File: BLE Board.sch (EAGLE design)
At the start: 34 parts, among them IC1 TM4C123GH6PM, IC2 TPS6300, J1 SAMTEC-FTSH-105-01-X-DVJ, Q1 NX5032GA

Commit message: First arrangement of components
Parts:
- removed PC4, PF0: (no value), EE445L:B3F-1052
- removed R6: 10k, EE445L:RESISTORR0402
- added C17, C19: 0.1uF, EE445L:CAPACITORC0402K
- added C18-T, C20-T: 4.7uF, EE445L:CAPACITORC0402K
- added R5: 10k, EE445L:RESISTORR0402
- added SW-PC4, SW-PF0: (no value), EE445L:B3F-1052
- C13, C14, C16: value 0.01uF -> 10uF
- C15: value 0.01uF -> 0.1uF
- R3: value 1M -> 100
- renumbered C4 to C4-T, J1 to BLE-DEBUG, Q1 to CRYS, S1 to RST, U$1 to BLE, U$2 to ON/OFF, U$3 to JTAG
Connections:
- net +3V3: now also C17.2, C18-T.2, C19.1, C20-T.1, SW-PC4.P, SW-PC4.P1, SW-PF0.P, SW-PF0.P1; no longer PC4.P, PC4.P1, PF0.P, PF0.P1
- net GND: now also C17.1, C18-T.1, C19.2, C20-T.2, R5.2; no longer R6.2
- net PF3: now also R5.1, SW-PF0.S, SW-PF0.S1; no longer PF0.S, PF0.S1, R6.1
- net PF4: now also SW-PC4.S, SW-PC4.S1; no longer PC4.S, PC4.S1
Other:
- moved on the sheet: DIS1, R4

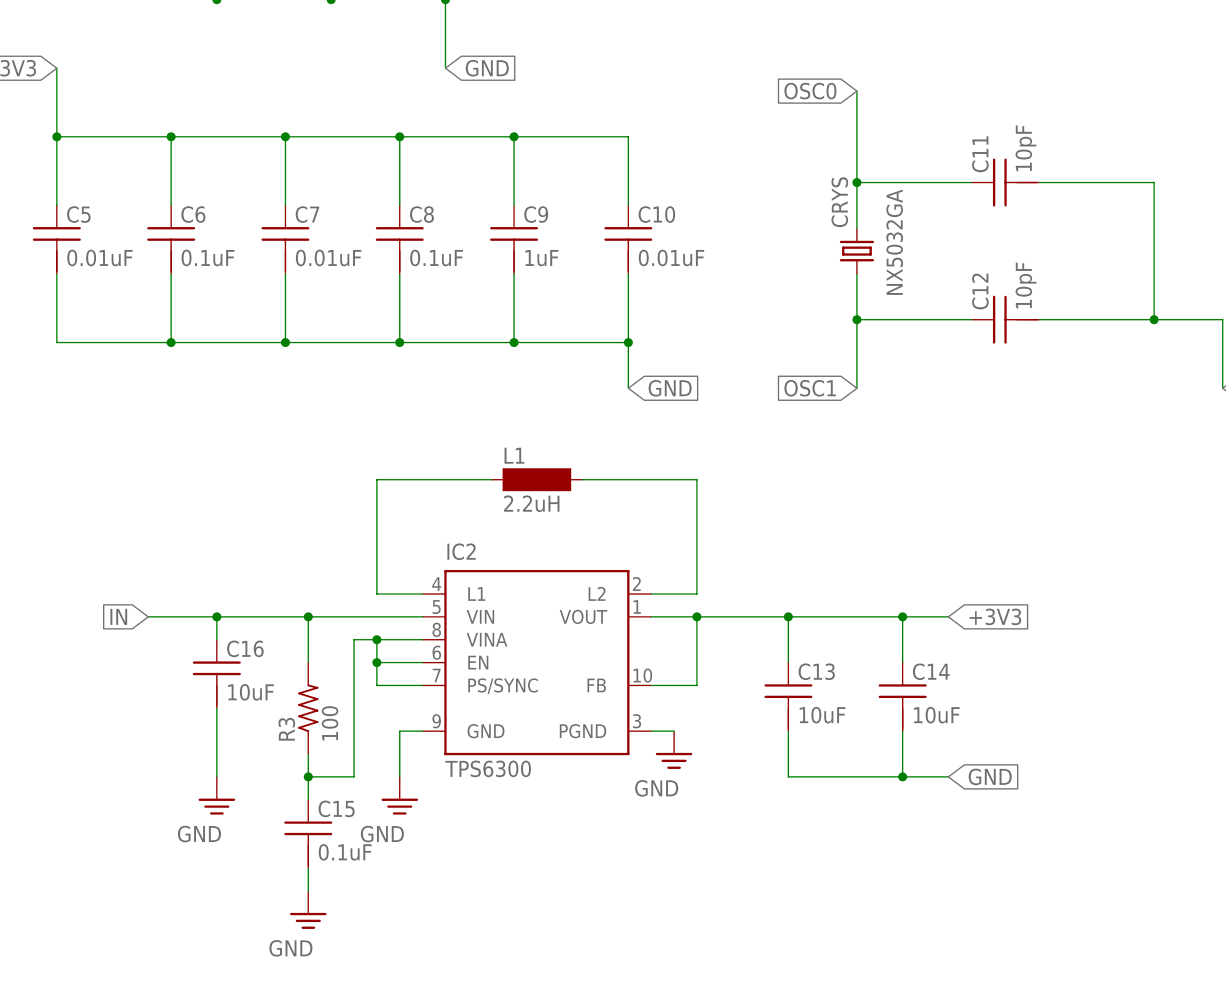
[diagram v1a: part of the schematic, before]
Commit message: Moved power reg., changed some parts
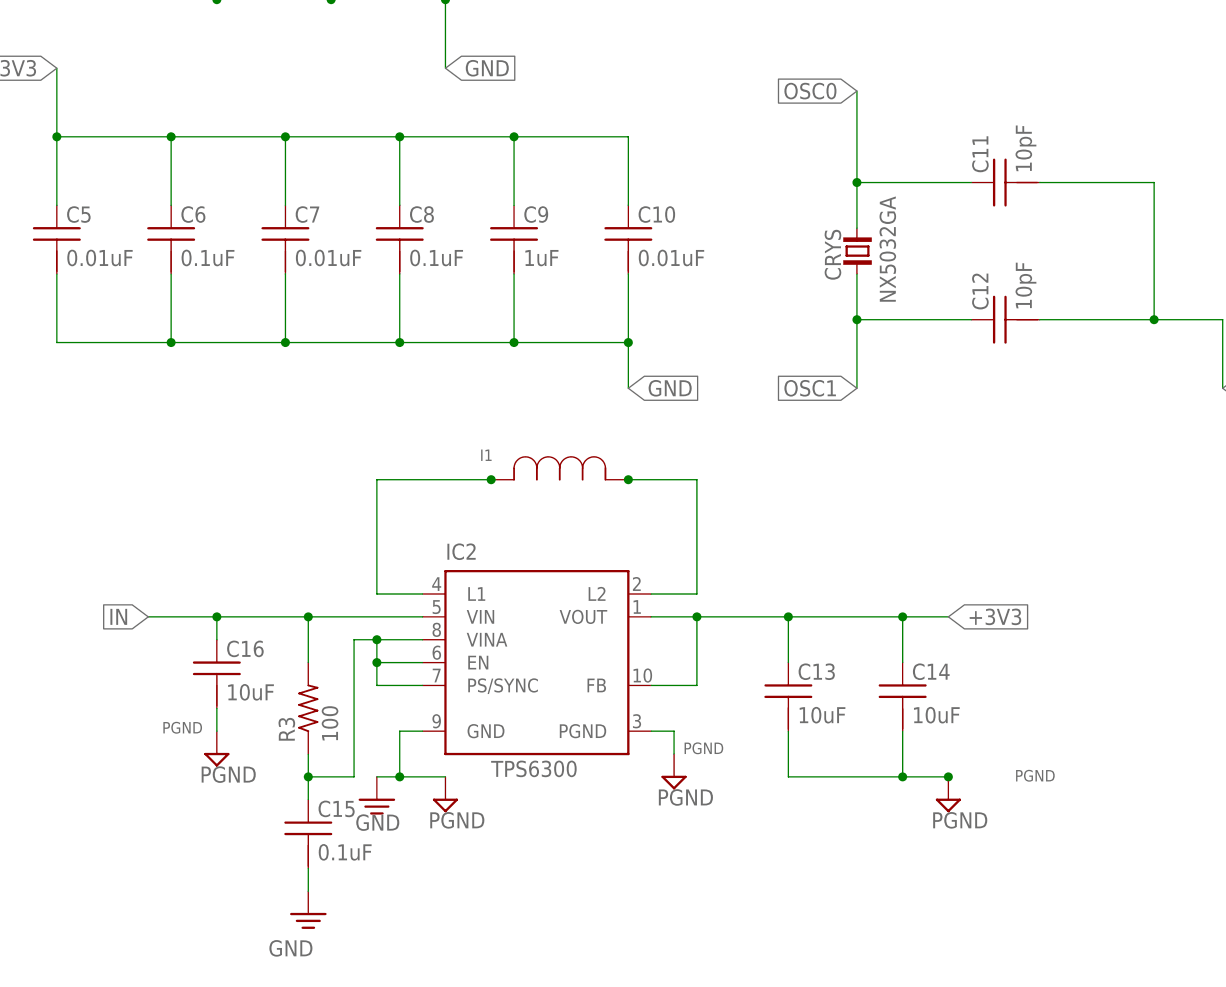
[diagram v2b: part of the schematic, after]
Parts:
- removed L1: 2.2uH, inductor-neosid:MS50
- added I1: (no value), 445L_final:IND_TPS
- CRYS: device EE445L:NX5032GA -> NX5032GA:NX5032GA
- R2, R3: device EE445L:RESISTORR0603 -> EE445L:RESISTORR0402
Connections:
- new net PGND: C13.2, C14.2, C16.2, IC2G$1.PGND
- net GND: no longer C13.2, C14.2, C16.2, IC2G$1.PGND
- net N$3: now also I1.2; no longer L1.1
- net N$4: now also I1.1; no longer L1.2

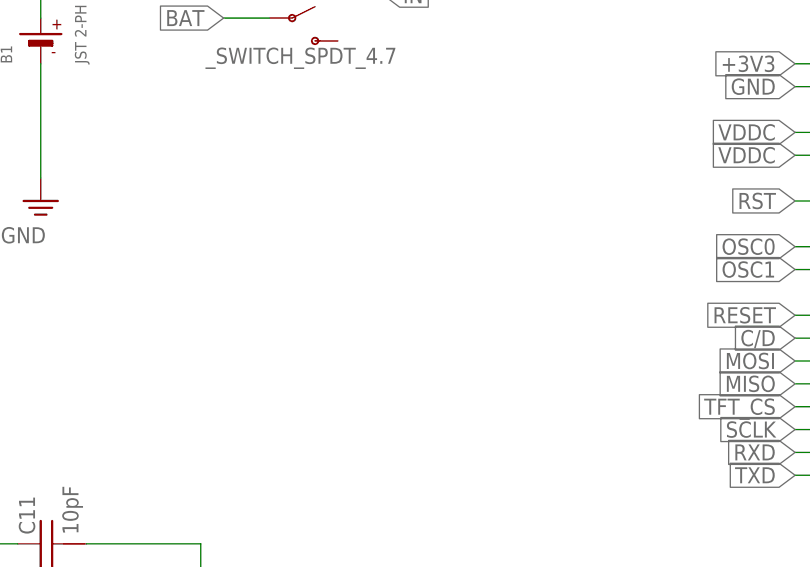
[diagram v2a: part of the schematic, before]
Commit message: 0603 cap/res, add test pts for gnd/pwr
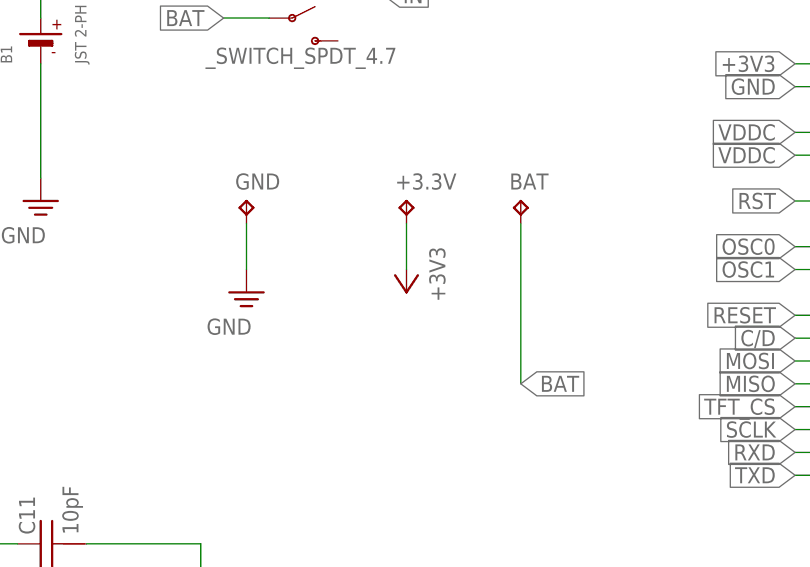
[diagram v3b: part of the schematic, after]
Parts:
- added +3.3V, BAT, GND: TP_KEYSTONE500X, EE445L:TP_KEYSTONE500X
- C1, C10, C11, C12, C13, C14, C15, C16, C17, C18-T, C19, C2, C20-T, C3, C4-T, C5, C6, C7, C8, C9: device EE445L:CAPACITORC0402K -> EE445L:CAPACITORC0603K
- R1, R2, R3, R4, R5: device EE445L:RESISTORR0402 -> EE445L:RESISTORR0603
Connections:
- net +3V3: now also +3.3V.TP
- net BAT: now also BAT.TP
- net GND: now also GND.TP
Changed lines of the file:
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@@
 <setting verticaltext="up"/>
 </settings>
-<grid distance="10" unitdist="mil" unit="mil" style="lines" multiple="1" display="no" altdistance="0.01" altunitdist="inch" altunit="inch"/>
+<grid distance="0.1" unitdist="inch" unit="inch" style="lines" multiple="1" display="no" altdistance="0.01" altunitdist="inch" altunit="inch"/>
 <layers>
 <layer number="1" name="Top" color="4" fill="1" visible="no" active="no"/>
@@
 <part name="+3V1" library="EE445L" deviceset="+3V3" device=""/>
 <part name="SUPPLY1" library="EE445L" deviceset="GND" device=""/>
-<part name="C1" library="EE445L" deviceset="CAPACITOR" device="C0402K" value="0.1uF"/>
-<part name="C2" library="EE445L" deviceset="CAPACITOR" device="C0402K" value="0.1uF"/>
-<part name="C3" library="EE445L" deviceset="CAPACITOR" device="C0402K" value="1uF"/>
-<part name="C5" library="EE445L" deviceset="CAPACITOR" device="C0402K" value="0.01uF"/>
-<part name="C6" library="EE445L" deviceset="CAPACITOR" device="C0402K" value="0.1uF"/>
-<part name="C7" library="EE445L" deviceset="CAPACITOR" device="C0402K" value="0.01uF"/>
-<part name="C8" library="EE445L" deviceset="CAPACITOR" device="C0402K" value="0.1uF"/>
-<part name="C9" library="EE445L" deviceset="CAPACITOR" device="C0402K" value="1uF"/>
-<part name="C10" library="EE445L" deviceset="CAPACITOR" device="C0402K" value="0.01uF"/>
+<part name="C1" library="EE445L" deviceset="CAPACITOR" device="C0603K" value="0.1uF"/>
+<part name="C2" library="EE445L" deviceset="CAPACITOR" device="C0603K" value="0.1uF"/>
+<part name="C3" library="EE445L" deviceset="CAPACITOR" device="C0603K" value="1uF"/>
+<part name="C5" library="EE445L" deviceset="CAPACITOR" device="C0603K" value="0.01uF"/>
+<part name="C6" library="EE445L" deviceset="CAPACITOR" device="C0603K" value="0.1uF"/>
+<part name="C7" library="EE445L" deviceset="CAPACITOR" device="C0603K" value="0.01uF"/>
+<part name="C8" library="EE445L" deviceset="CAPACITOR" device="C0603K" value="0.1uF"/>
+<part name="C9" library="EE445L" deviceset="CAPACITOR" device="C0603K" value="1uF"/>
+<part name="C10" library="EE445L" deviceset="CAPACITOR" device="C0603K" value="0.01uF"/>
 <part name="RST" library="EE445L" deviceset="B3F-1052" device=""/>
-<part name="R1" library="EE445L" deviceset="RESISTOR" device="R0402" value="10k"/>
-<part name="C11" library="EE445L" deviceset="CAPACITOR" device="C0402K" value="10pF"/>
-<part name="C12" library="EE445L" deviceset="CAPACITOR" device="C0402K" value="10pF"/>
-<part name="C4-T" library="EE445L" deviceset="CAPACITOR" device="C0402K" value="2.2uF"/>
-<part name="C13" library="EE445L" deviceset="CAPACITOR" device="C0402K" value="10uF"/>
-<part name="C14" library="EE445L" deviceset="CAPACITOR" device="C0402K" value="10uF"/>
-<part name="C15" library="EE445L" deviceset="CAPACITOR" device="C0402K" value="0.1uF"/>
-<part name="C16" library="EE445L" deviceset="CAPACITOR" device="C0402K" value="10uF"/>
+<part name="R1" library="EE445L" deviceset="RESISTOR" device="R0603" value="10k"/>
+<part name="C11" library="EE445L" deviceset="CAPACITOR" device="C0603K" value="10pF"/>
+<part name="C12" library="EE445L" deviceset="CAPACITOR" device="C0603K" value="10pF"/>
+<part name="C4-T" library="EE445L" deviceset="CAPACITOR" device="C0603K" value="2.2uF"/>
+<part name="C13" library="EE445L" deviceset="CAPACITOR" device="C0603K" value="10uF"/>
+<part name="C14" library="EE445L" deviceset="CAPACITOR" device="C0603K" value="10uF"/>
+<part name="C15" library="EE445L" deviceset="CAPACITOR" device="C0603K" value="0.1uF"/>
+<part name="C16" library="EE445L" deviceset="CAPACITOR" device="C0603K" value="10uF"/>
 <part name="SUPPLY3" library="EE445L" deviceset="GND" device=""/>
 <part name="B1" library="microbuilder" deviceset="BATTERY" device="" value="JST 2-PH"/>
@@
 <part name="DIS1" library="EE445L" deviceset="ST7735" device=""/>
 <part name="SW-PC4" library="EE445L" deviceset="B3F-1052" device=""/>
-<part name="R4" library="EE445L" deviceset="RESISTOR" device="R0402" value="10k"/>
+<part name="R4" library="EE445L" deviceset="RESISTOR" device="R0603" value="10k"/>
 <part name="SW-PF0" library="EE445L" deviceset="B3F-1052" device=""/>
-<part name="R5" library="EE445L" deviceset="RESISTOR" device="R0402" value="10k"/>
+<part name="R5" library="EE445L" deviceset="RESISTOR" device="R0603" value="10k"/>
 <part name="BLE-DEBUG" library="SAMTEC-FTSH-105-01-X-DV" deviceset="SAMTEC-FTSH-105-01-X-DV" device="J"/>
 <part name="BLE" library="zyongye" deviceset="BGM220P" device=""/>
 <part name="ON/OFF" library="Z" deviceset="_SWITCH_SPDT_4.7" device=""/>
 <part name="JTAG" library="Z" deviceset="JTAG_SERIAL" device=""/>
-<part name="C19" library="EE445L" deviceset="CAPACITOR" device="C0402K" value="0.1uF"/>
-<part name="C20-T" library="EE445L" deviceset="CAPACITOR" device="C0402K" value="4.7uF"/>
-<part name="C17" library="EE445L" deviceset="CAPACITOR" device="C0402K" value="0.1uF"/>
-<part name="C18-T" library="EE445L" deviceset="CAPACITOR" device="C0402K" value="4.7uF"/>
+<part name="C19" library="EE445L" deviceset="CAPACITOR" device="C0603K" value="0.1uF"/>
+<part name="C20-T" library="EE445L" deviceset="CAPACITOR" device="C0603K" value="4.7uF"/>
+<part name="C17" library="EE445L" deviceset="CAPACITOR" device="C0603K" value="0.1uF"/>
+<part name="C18-T" library="EE445L" deviceset="CAPACITOR" device="C0603K" value="4.7uF"/>
 <part name="I1" library="445L_final" deviceset="IND_TPS" device=""/>
 <part name="SUPPLY7" library="supply2" library_urn="urn:adsk.eagle:library:372" deviceset="GND" device="" value="PGND"/>
@@
 <part name="SUPPLY9" library="supply2" library_urn="urn:adsk.eagle:library:372" deviceset="GND" device="" value="PGND"/>
 <part name="SUPPLY10" library="supply2" library_urn="urn:adsk.eagle:library:372" deviceset="GND" device="" value="PGND"/>
-<part name="R3" library="EE445L" deviceset="RESISTOR" device="R0402" value="100"/>
-<part name="R2" library="EE445L" deviceset="RESISTOR" device="R0402" value="1M"/>
+<part name="R3" library="EE445L" deviceset="RESISTOR" device="R0603" value="100"/>
+<part name="R2" library="EE445L" deviceset="RESISTOR" device="R0603" value="1M"/>
 <part name="CRYS" library="NX5032GA" deviceset="NX5032GA" device=""/>
+<part name="GND" library="EE445L" deviceset="TP" device="_KEYSTONE500X"/>
+<part name="+3.3V" library="EE445L" deviceset="TP" device="_KEYSTONE500X"/>
+<part name="SUPPLY2" library="EE445L" deviceset="GND" device=""/>
+<part name="+3V2" library="EE445L" deviceset="+3V3" device=""/>
+<part name="BAT" library="EE445L" deviceset="TP" device="_KEYSTONE500X"/>
 </parts>
 <sheets>
@@
 <attribute name="VALUE" x="-13.462" y="72.898" size="1.778" layer="96" rot="R90"/>
 </instance>
+<instance part="GND" gate="G$1" x="20.32" y="124.46" smashed="yes">
+<attribute name="NAME" x="19.05" y="125.73" size="1.778" layer="95"/>
+<attribute name="TP_SIGNAL_NAME" x="21.59" y="123.19" size="1.778" layer="97"/>
+</instance>
+<instance part="+3.3V" gate="G$1" x="38.1" y="124.46" smashed="yes">
+<attribute name="NAME" x="36.83" y="125.73" size="1.778" layer="95"/>
+<attribute name="TP_SIGNAL_NAME" x="39.37" y="123.19" size="1.778" layer="97"/>
+</instance>
+<instance part="SUPPLY2" gate="GND" x="20.32" y="114.3" smashed="yes">
+<attribute name="VALUE" x="15.875" y="109.601" size="1.778" layer="96"/>
+</instance>
+<instance part="+3V2" gate="G$1" x="38.1" y="114.3" smashed="yes" rot="R180">
+<attribute name="VALUE" x="40.64" y="119.38" size="1.778" layer="96" rot="R270"/>
+</instance>
+<instance part="BAT" gate="G$1" x="50.8" y="124.46" smashed="yes">
+<attribute name="NAME" x="49.53" y="125.73" size="1.778" layer="95"/>
+<attribute name="TP_SIGNAL_NAME" x="52.07" y="123.19" size="1.778" layer="97"/>
+</instance>
 </instances>
 <busses>
@@
 <label x="284.48" y="86.36" size="1.778" layer="95" rot="R90" xref="yes"/>
 </segment>
+<segment>
+<pinref part="+3V2" gate="G$1" pin="+3V3"/>
+<wire x1="38.1" y1="116.84" x2="38.1" y2="121.92" width="0.1524" layer="91"/>
+<pinref part="+3.3V" gate="G$1" pin="TP"/>
+</segment>
 </net>
 <net name="GND" class="0">
@@
 <junction x="-68.58" y="20.32"/>
 </segment>
+<segment>
+<pinref part="GND" gate="G$1" pin="TP"/>
+<pinref part="SUPPLY2" gate="GND" pin="GND"/>
+<wire x1="20.32" y1="121.92" x2="20.32" y2="116.84" width="0.1524" layer="91"/>
+</segment>
 </net>
 <net name="VDDC" class="0">
@@
 <label x="17.78" y="144.78" size="1.778" layer="95" rot="R180" xref="yes"/>
 </segment>
-</net>
+<segment>
+<wire x1="50.8" y1="121.92" x2="50.8" y2="104.14" width="0.1524" layer="91"/>
+<label x="50.8" y="104.14" size="1.778" layer="95" xref="yes"/>
+<pinref part="BAT" gate="G$1" pin="TP"/>
+</segment>
+</net>
